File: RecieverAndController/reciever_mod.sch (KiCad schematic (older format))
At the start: 24 parts

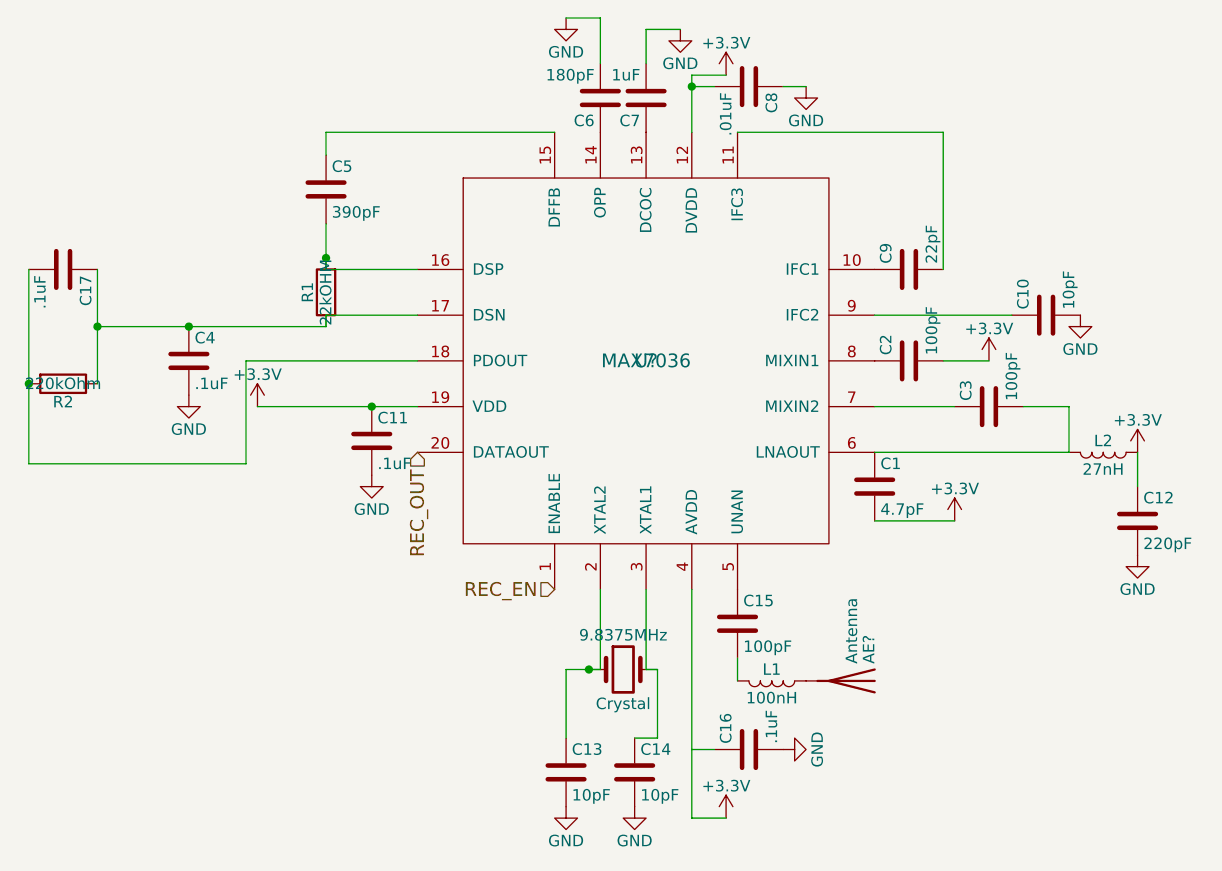
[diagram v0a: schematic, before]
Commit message: adding footprints to schematic
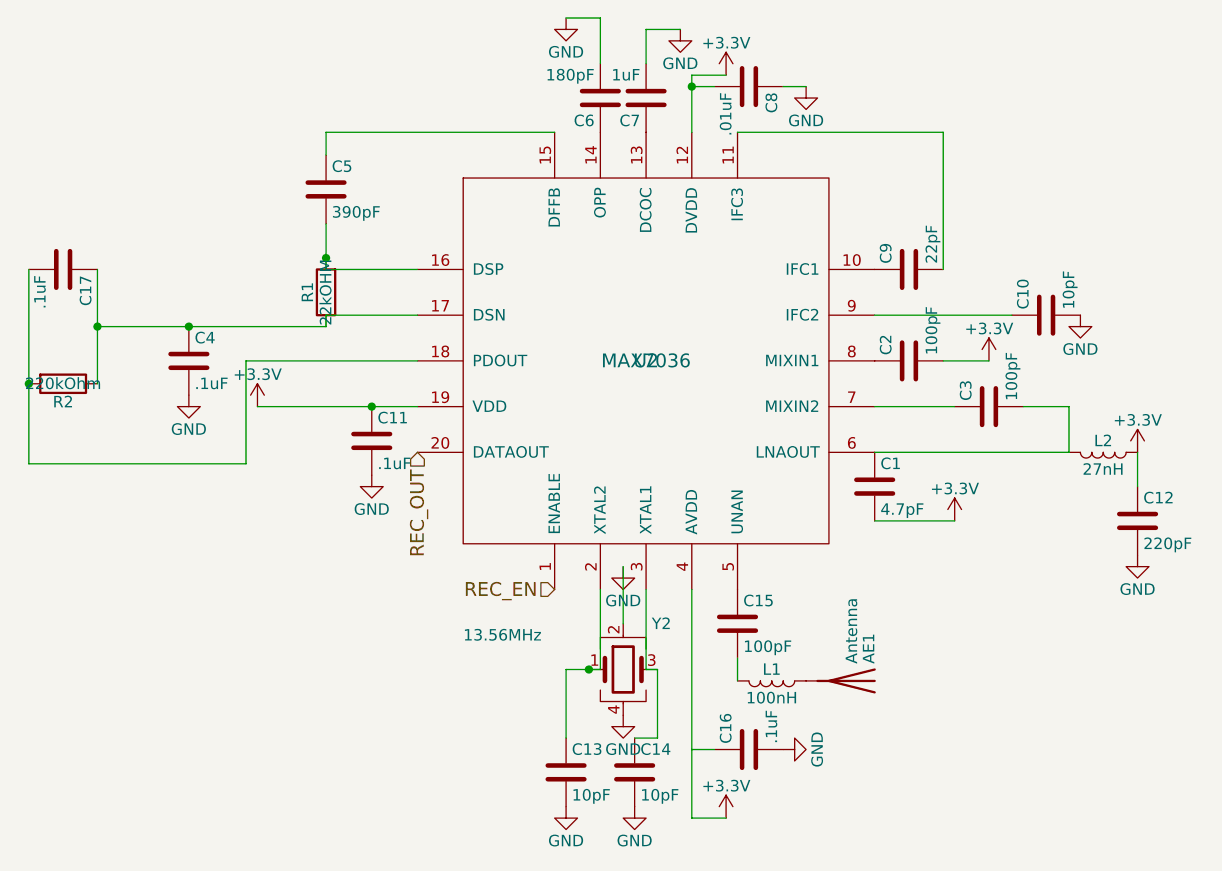
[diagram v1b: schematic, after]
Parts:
- removed 9.8375MHz: Crystal, symbol Crystal
- added Y2: 13.56MHz, Custom:1253-1737-1-ND, symbol Crystal_GND24
- AE1: renamed from AE?; footprint (none) -> Custom:311-1570-1-ND
- C1, C10, C11, C12, C13, C14, C15, C16, C17, C2, C3, C4, C5, C6, C7, C8, C9: footprint (none) -> Capacitors_SMD:C_0603
- L1, L2: footprint (none) -> Inductors_SMD:L_0603
- R1, R2: footprint (none) -> Resistors_SMD:R_0603
- U2: renamed from U?; footprint (none) -> Custom:MAX7036GTP
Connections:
- net GND: now also Y2.2, Y2.4
- net at C13.1, U2.2 (XTAL2): now also Y2.1
- net at C14.1, U2.3 (XTAL1): now also Y2.3
